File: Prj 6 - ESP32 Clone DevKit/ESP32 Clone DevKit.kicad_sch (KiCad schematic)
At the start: 34 parts, among them J1 USB CON8, J2 Conn_01x19_Pin, J3 Conn_01x19_Pin, Q1 MMSS8050-H-TP, Q2 MMSS8050-H-TP, SW1 SW_Push, SW2 SW_Push, U1 CP2102N-A01-GQFN28, U2 AMS1117-3.3, U3 ESP32-WROOM-32D

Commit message: Completed most of PCB Editor parameters and constrais
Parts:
- R11, R17, R21, R22, R23, R25, R26: footprint (none) -> Resistor_SMD:R_01005_0402Metric_Pad0.57x0.30mm_HandSolder
- SW1, SW2: footprint (none) -> Button_Switch_SMD:SW_SPST_B3S-1000
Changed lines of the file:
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@@
 			)
 		)
-		(property "Footprint" ""
+		(property "Footprint" "Resistor_SMD:R_01005_0402Metric_Pad0.57x0.30mm_HandSolder"
 			(at 101.092 118.11 90)
 			(effects
@@
 			)
 		)
-		(property "Footprint" ""
+		(property "Footprint" "Resistor_SMD:R_01005_0402Metric_Pad0.57x0.30mm_HandSolder"
 			(at 161.29 127.508 90)
 			(effects
@@
 			)
 		)
-		(property "Footprint" ""
+		(property "Footprint" "Button_Switch_SMD:SW_SPST_B3S-1000"
 			(at 135.89 17.78 0)
 			(effects
@@
 			)
 		)
-		(property "Footprint" ""
+		(property "Footprint" "Resistor_SMD:R_01005_0402Metric_Pad0.57x0.30mm_HandSolder"
 			(at 261.112 63.5 90)
 			(effects
@@
 			)
 		)
-		(property "Footprint" ""
+		(property "Footprint" "Resistor_SMD:R_01005_0402Metric_Pad0.57x0.30mm_HandSolder"
 			(at 95.25 114.808 90)
 			(effects
@@
 			)
 		)
-		(property "Footprint" ""
+		(property "Footprint" "Button_Switch_SMD:SW_SPST_B3S-1000"
 			(at 135.89 36.83 0)
 			(effects
@@
 			)
 		)
-		(property "Footprint" ""
+		(property "Footprint" "Resistor_SMD:R_01005_0402Metric_Pad0.57x0.30mm_HandSolder"
 			(at 49.53 118.618 90)
 			(effects
@@
 			)
 		)
-		(property "Footprint" ""
+		(property "Footprint" "Resistor_SMD:R_01005_0402Metric_Pad0.57x0.30mm_HandSolder"
 			(at 38.1 137.668 90)
 			(effects
@@
 			)
 		)
-		(property "Footprint" ""
+		(property "Footprint" "Resistor_SMD:R_01005_0402Metric_Pad0.57x0.30mm_HandSolder"
 			(at 38.1 152.908 90)
 			(effects

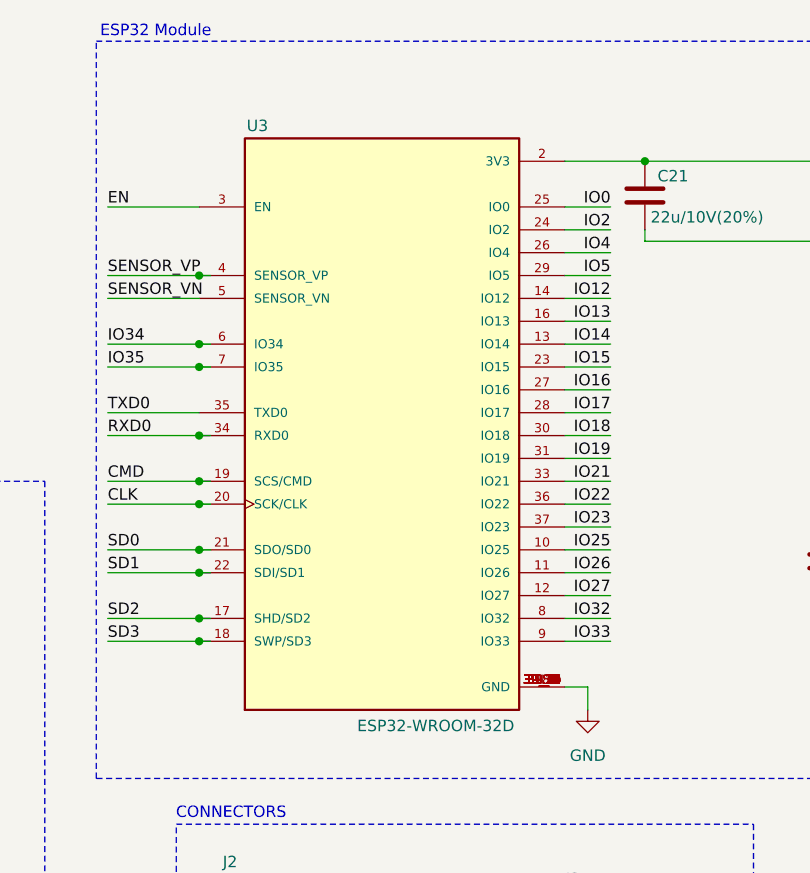
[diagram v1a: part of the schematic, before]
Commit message: Trying to do differential tracks
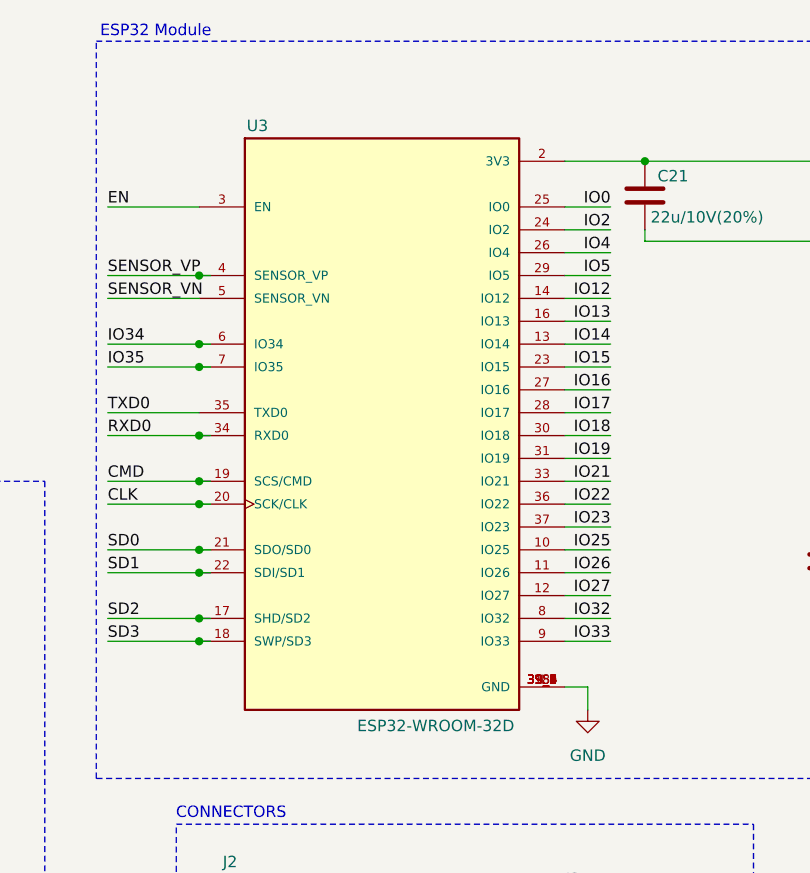
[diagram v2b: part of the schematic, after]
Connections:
- net GND: no longer U3.39_10 (GND), U3.39_11 (GND), U3.39_12 (GND), U3.39_13 (GND), U3.39_14 (GND), U3.39_15 (GND), U3.39_16 (GND), U3.39_17 (GND), U3.39_18 (GND), U3.39_19 (GND), U3.39_20 (GND), U3.39_21 (GND)
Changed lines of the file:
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@@
+			)
+		)
+		(property "Purpose" ""
+			(at 213.36 57.15 0)
+			(effects
+				(font
+					(size 1.27 1.27)
+				)
+			)
+		)
+		(property "Field-1" ""
+			(at 213.36 57.15 0)
+			(effects
+				(font
+					(size 1.27 1.27)
+				)
 			)
 		)
@@
 		(pin "31"
 		)
-		(pin "39_17"
-		)
-		(pin "39_13"
-		)
 		(pin "1"
-		)
-		(pin "39_18"
 		)
 		(pin "19"
@@
 		)
 		(pin "29"
-		)
-		(pin "39_14"
-		)
-		(pin "39_16"
-		)
-		(pin "39_19"
 		)
 		(pin "16"
@@
 		(pin "26"
 		)
-		(pin "39_11"
-		)
 		(pin "39_2"
 		)
-		(pin "39_20"
-		)
 		(pin "24"
-		)
-		(pin "39_21"
 		)
 		(pin "39_4"
@@
 		(pin "39_9"
 		)
-		(pin "39_12"
-		)
-		(pin "39_10"
-		)
-		(pin "39_15"
-		)
 		(pin "34"
